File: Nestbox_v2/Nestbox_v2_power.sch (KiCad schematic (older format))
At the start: 47 parts, among them U201 bq25504, U202 TPS63051, U203 TPS63050

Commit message: created V2 MLX breakout board
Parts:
- removed BT201: Battery, Connectors_Molex:Molex_KK-6410-02_02x2.54mm_Straight, symbol Battery-RESCUE-Nestbox_v1
- removed C201, C202, C203: C, symbol C
- removed D201, D202: LED, symbol LED
- removed JP201: Jumper, symbol Jumper
- removed L201: L, symbol L
- removed R203, R206, R207, R208, R209, R210, R212, R213, R214, R221, R222: R, symbol R
- removed R211: 1E, symbol R
- removed SC201: Solar_Cells, symbol Solar_Cells
- removed U201: bq25504, symbol bq25504-RESCUE-Nestbox_v2
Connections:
- net labels removed: BAT_OK, HK_SOLAR_I
- wire segments 136 -> 102
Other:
- note removed: "OT_PROG to GND means 60° temp limit\nTO REVIEW"
- note removed: "is this for solar current measurement?\nmay be useful to use low-ohmic 4-terminal\n current sense resistor and a pre-amp"
- moved on the sheet: C204, C205, C206, C207, C208, C209, C210, JP202, JP203, JP204, JP205, L202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

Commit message: restructured top level sheet with hierarchical labels, assigned most GPIOs
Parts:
- removed R215, R216: R, symbol R
- added J?: CONN_01X02, symbol CONN_01X02
- added U?: LP5907, TO_SOT_Packages_SMD:SOT-23-5, symbol LD3985M
- R201, R202, R204, R205: value R -> 1M 1%
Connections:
- net labels added: +3V3, 5V_ENABLE, HK_5V_V, LDO_EN, VAA
- net labels removed: 5V_Enable, HK_BUS_V, HK_SOLAR_V, PGOOD_3.3, PGOOD_5, VBus, VSolar
- wire segments 102 -> 101
- no-connect marks 0 -> 1
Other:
- note added: "TODO: add battery undervoltage protection circuit!\n(to enable pin!)\n\nOther option: Use 2 cell alkaline battery."
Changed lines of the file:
@@
 LIBS:SeeedOPL-Transistor-2016
 LIBS:Nestbox_v2-cache
-EELAYER 26 0
+EELAYER 25 0
 EELAYER END
 $Descr A4 11693 8268
@@
 	3050 1700 2900 1700
 Wire Wire Line
-	2900 1700 2900 1900
-Wire Wire Line
 	2400 1900 2700 1900
 Wire Wire Line
 	2700 1900 2900 1900
 Wire Wire Line
-	2900 1900 3050 1900
+	2900 1900 2950 1900
+Wire Wire Line
+	2950 1900 3050 1900
 Connection ~ 2900 1900
 Text Label 1250 1900 0    60   ~ 0
-VBus
+VBat
 Wire Wire Line
 	3050 2400 3000 2400
@@
 	0    1    1    0
 $EndComp
-Text GLabel 4600 1350 2    60   Input ~ 0
-PGOOD_3.3
-Wire Wire Line
-	4500 1700 4500 1350
-Wire Wire Line
-	4500 1350 4600 1350
 Connection ~ 4500 1700
 Wire Wire Line
@@
 	6000 4150 6300 4150
 Connection ~ 4950 4150
-Wire Wire Line
-	4500 3950 4500 3600
-Wire Wire Line
-	4500 3600 4600 3600
 Connection ~ 4500 3950
 Wire Wire Line
@@
 	4450 4650 4550 4650
 Connection ~ 4550 4750
-Text GLabel 4600 3600 2    60   Input ~ 0
-PGOOD_5
 $Comp
 L +5V #PWR019
@@
 	5000 4750 4750 4750
 Connection ~ 4750 4750
-Text GLabel 2900 3950 0    60   Input ~ 0
-5V_Enable
 $Comp
 L C C205
@@
 	1800 4150 1550 4150
 Text Label 1550 4150 0    60   ~ 0
-VBus
+VBat
 $Comp
 L R R201
@@
 P 8650 1600
 F 0 "R201" H 8720 1646 50  0000 L CNN
-F 1 "R" H 8720 1555 50  0000 L CNN
+F 1 "1M 1%" H 8720 1555 50  0000 L CNN
 F 2 "" V 8580 1600 50  0001 C CNN
 F 3 "" H 8650 1600 50  0001 C CNN
@@
 P 8650 2000
 F 0 "R204" H 8720 2046 50  0000 L CNN
-F 1 "R" H 8720 1955 50  0000 L CNN
+F 1 "1M 1%" H 8720 1955 50  0000 L CNN
 F 2 "" V 8580 2000 50  0001 C CNN
 F 3 "" H 8650 2000 50  0001 C CNN
@@
 	1    0    0    -1
 $EndComp
-Wire Wire Line
-	8650 1150 8650 1450
 Wire Wire Line
 	8650 1750 8650 1800
@@
 	1    0    0    -1
 $EndComp
-Text GLabel 8800 1800 2    60   Input ~ 0
-HK_BUS_V
 Wire Wire Line
 	8650 1800 8800 1800
 Connection ~ 8650 1800
-Text Label 8650 1150 3    60   ~ 0
-VBus
 $Comp
 L R R202
@@
 P 9850 1600
 F 0 "R202" H 9920 1646 50  0000 L CNN
-F 1 "R" H 9920 1555 50  0000 L CNN
+F 1 "1M 1%" H 9920 1555 50  0000 L CNN
 F 2 "" V 9780 1600 50  0001 C CNN
 F 3 "" H 9850 1600 50  0001 C CNN
@@
 P 9850 2000
 F 0 "R205" H 9920 2046 50  0000 L CNN
-F 1 "R" H 9920 1955 50  0000 L CNN
+F 1 "1M 1%" H 9920 1955 50  0000 L CNN
 F 2 "" V 9780 2000 50  0001 C CNN
 F 3 "" H 9850 2000 50  0001 C CNN
@@
 	1    0    0    -1
 $EndComp
-Text GLabel 10000 1800 2    60   Input ~ 0
-HK_BAT_V
 Wire Wire Line
 	9850 1800 10000 1800
@@
 Text Label 9850 1150 3    60   ~ 0
 VBat
-$Comp
-L R R215
-U 1 1 5A02E91F
-P 9850 3000
-F 0 "R215" H 9920 3046 50  0000 L CNN
-F 1 "R" H 9920 2955 50  0000 L CNN
-F 2 "" V 9780 3000 50  0001 C CNN
-F 3 "" H 9850 3000 50  0001 C CNN
-	1    9850 3000
-	1    0    0    -1
-$EndComp
-$Comp
-L R R216
-U 1 1 5A02E925
-P 9850 3400
-F 0 "R216" H 9920 3446 50  0000 L CNN
-F 1 "R" H 9920 3355 50  0000 L CNN
-F 2 "" V 9780 3400 50  0001 C CNN
-F 3 "" H 9850 3400 50  0001 C CNN
-	1    9850 3400
-	1    0    0    -1
-$EndComp
-Wire Wire Line
-	9850 2550 9850 2850
-Wire Wire Line
-	9850 3150 9850 3200
-Wire Wire Line
-	9850 3200 9850 3250
-Wire Wire Line
-	9850 3550 9850 3600
-$Comp
-L GND #PWR025
-U 1 1 5A02E92E
-P 9850 3600
-F 0 "#PWR025" H 9850 3350 50  0001 C CNN
-F 1 "GND" H 9855 3427 50  0000 C CNN
-F 2 "" H 9850 3600 50  0001 C CNN
-F 3 "" H 9850 3600 50  0001 C CNN
-	1    9850 3600
-	1    0    0    -1
-$EndComp
-Text GLabel 10000 3200 2    60   Input ~ 0
-HK_SOLAR_V
-Wire Wire Line
-	9850 3200 10000 3200
-Connection ~ 9850 3200
-Text Label 9850 2550 3    60   ~ 0
-VSolar
+Text HLabel 2900 3950 0    60   Input ~ 0
+5V_ENABLE
+$Comp
+L +5V #PWR?
+U 1 1 5B070A76
+P 8650 1300
+F 0 "#PWR?" H 8650 1150 50  0001 C CNN
+F 1 "+5V" V 8665 1428 50  0000 L CNN
+F 2 "" H 8650 1300 50  0001 C CNN
+F 3 "" H 8650 1300 50  0001 C CNN
+	1    8650 1300
+	1    0    0    -1
+$EndComp
+Wire Wire Line
+	8650 1450 8650 1300
+Text HLabel 8800 1800 2    60   Input ~ 0
+HK_5V_V
+Text HLabel 10000 1800 2    60   Input ~ 0
+HK_BAT_V
+Text Notes 700  1450 0    60   ~ 0
+TODO: add battery undervoltage protection circuit!\n(to enable pin!)\n\nOther option: Use 2 cell alkaline battery.
+Wire Wire Line
+	2900 1700 2900 1900
+Wire Wire Line
+	2900 1900 2950 1900
+Connection ~ 2950 1900
+$Comp
+L CONN_01X02 J?
+U 1 1 5B072802
+P 8850 3200
+F 0 "J?" H 8850 3350 50  0000 C CNN
+F 1 "CONN_01X02" V 8950 3200 50  0000 C CNN
+F 2 "" H 8850 3200 50  0001 C CNN
+F 3 "" H 8850 3200 50  0001 C CNN
+	1    8850 3200
+	1    0    0    -1
+$EndComp
+Wire Wire Line
+	8650 3150 8350 3150
+Wire Wire Line
+	8650 3250 8400 3250
+Wire Wire Line
+	8400 3250 8400 3400
+$Comp
+L GND #PWR?
+U 1 1 5B072B3F
+P 8400 3400
+F 0 "#PWR?" H 8400 3150 50  0001 C CNN
+F 1 "GND" H 8400 3250 50  0000 C CNN
+F 2 "" H 8400 3400 50  0001 C CNN
+F 3 "" H 8400 3400 50  0001 C CNN
+	1    8400 3400
+	1    0    0    -1
+$EndComp
+Text Label 8350 3150 0    60   ~ 0
+VBat
+$Comp
+L LD3985M U?
+U 1 1 5B0757BD
+P 3600 6400
+F 0 "U?" H 3600 6715 50  0000 C CNN
+F 1 "LP5907" H 3600 6624 50  0000 C CNN
+F 2 "TO_SOT_Packages_SMD:SOT-23-5" H 3500 6150 50  0001 C CNN
+F 3 "" H 3600 6400 50  0001 C CNN
+	1    3600 6400
+	1    0    0    -1
+$EndComp
+$Comp
+L +3V3 #PWR?
+U 1 1 5B0757C4
+P 2900 6350
+F 0 "#PWR?" H 2900 6200 50  0001 C CNN
+F 1 "+3V3" H 2915 6523 50  0000 C CNN
+F 2 "" H 2900 6350 50  0001 C CNN
+F 3 "" H 2900 6350 50  0001 C CNN
+	1    2900 6350
+	1    0    0    -1
+$EndComp
+$Comp
+L GND #PWR?
+U 1 1 5B0757CA
+P 3600 6800
+F 0 "#PWR?" H 3600 6550 50  0001 C CNN
+F 1 "GND" H 3605 6627 50  0000 C CNN
+F 2 "" H 3600 6800 50  0001 C CNN
+F 3 "" H 3600 6800 50  0001 C CNN
+	1    3600 6800
+	1    0    0    -1
+$EndComp
+NoConn ~ 4100 6450
+$Comp
+L VAA #PWR?
+U 1 1 5B0757D1
+P 4350 6350
+F 0 "#PWR?" H 4350 6200 50  0001 C CNN
+F 1 "VAA" H 4367 6523 50  0000 C CNN
+F 2 "" H 4350 6350 50  0001 C CNN
+F 3 "" H 4350 6350 50  0001 C CNN
+	1    4350 6350
+	1    0    0    -1
+$EndComp
+Wire Wire Line
+	2900 6350 3100 6350
+Wire Wire Line
+	3100 6450 2900 6450
+Wire Wire Line
+	4100 6350 4350 6350
+Text HLabel 2900 6450 0    60   Input ~ 0
+LDO_EN
 $EndSCHEMATC

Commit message: finished power supply schematics
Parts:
- removed C206: 10u, symbol C
- removed C210: 10p, symbol C
- removed R201, R202, R204, R205: 1M 1%, symbol R
- removed R217: 1M, symbol R
- removed U202: TPS63051, symbol TPS63051
- removed U203: TPS63050, symbol TPS63050
- added C? (x2): 1u, symbol C
- added R?: 100k, symbol R
- added R?: 50k, symbol R
- added U?: TPS62745, symbol TPS62745
- added U?: TPS62125, symbol TPS62125
- L203: value 1.5u -> 10uH
- R219: value R -> 1M1
- R220: value R -> 210k
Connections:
- net labels added: +BATT, 5V_PG, BAT_TEST_ENABLE, Vbat
- net labels removed: HK_5V_V
- wire segments 101 -> 81
- no-connect marks 1 -> 3
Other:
- note removed: "ILIM0 = Low <- 0.65*Iin_max"
- note removed: "SS floating for default Soft-Start time"
- moved on the sheet: C204, JP202, L202, L203, R218, R220

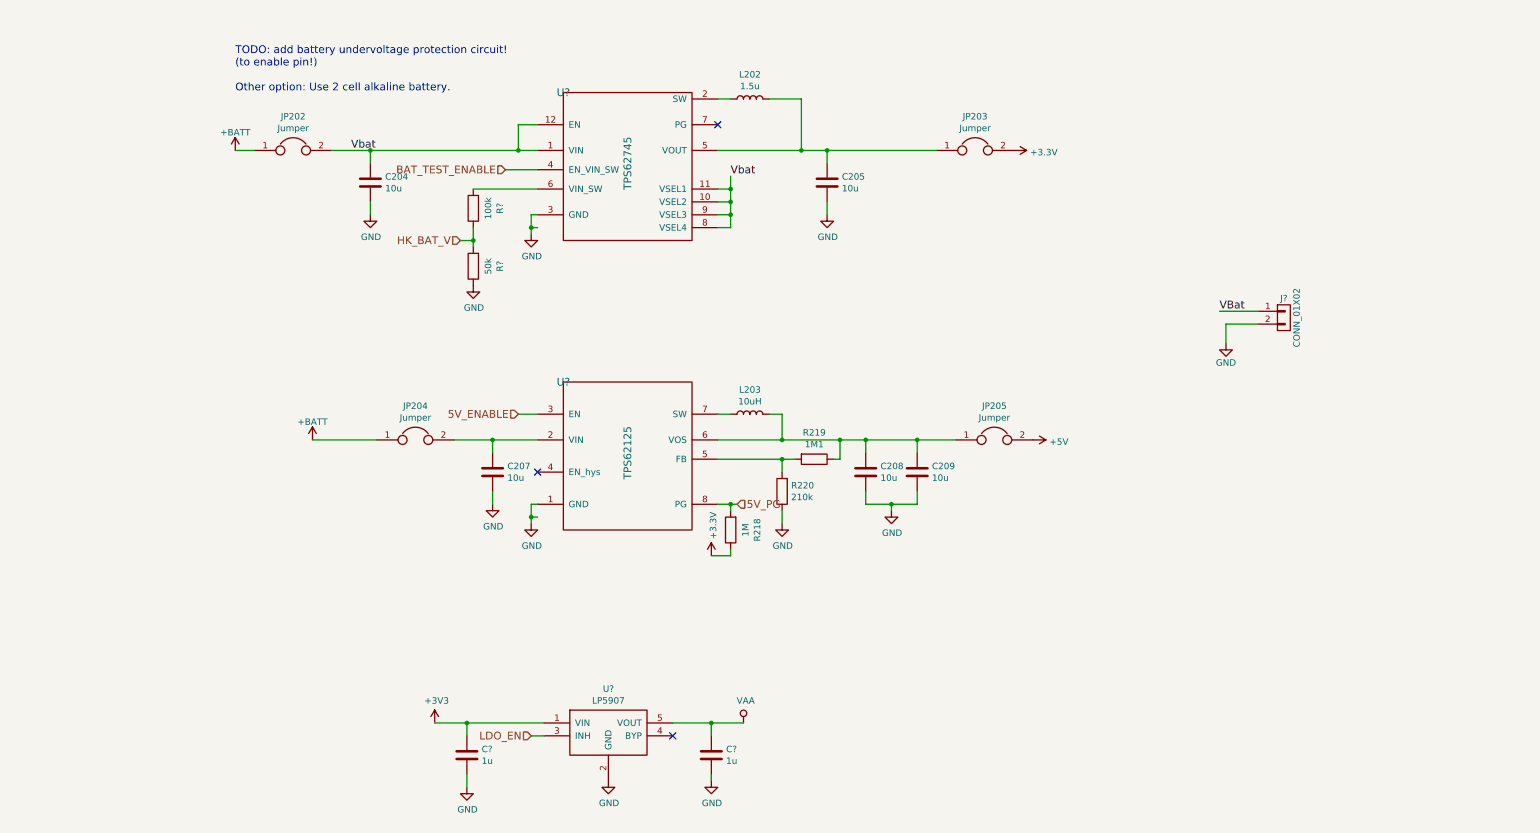
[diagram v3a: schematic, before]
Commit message: added PIR and lightbarrier headers
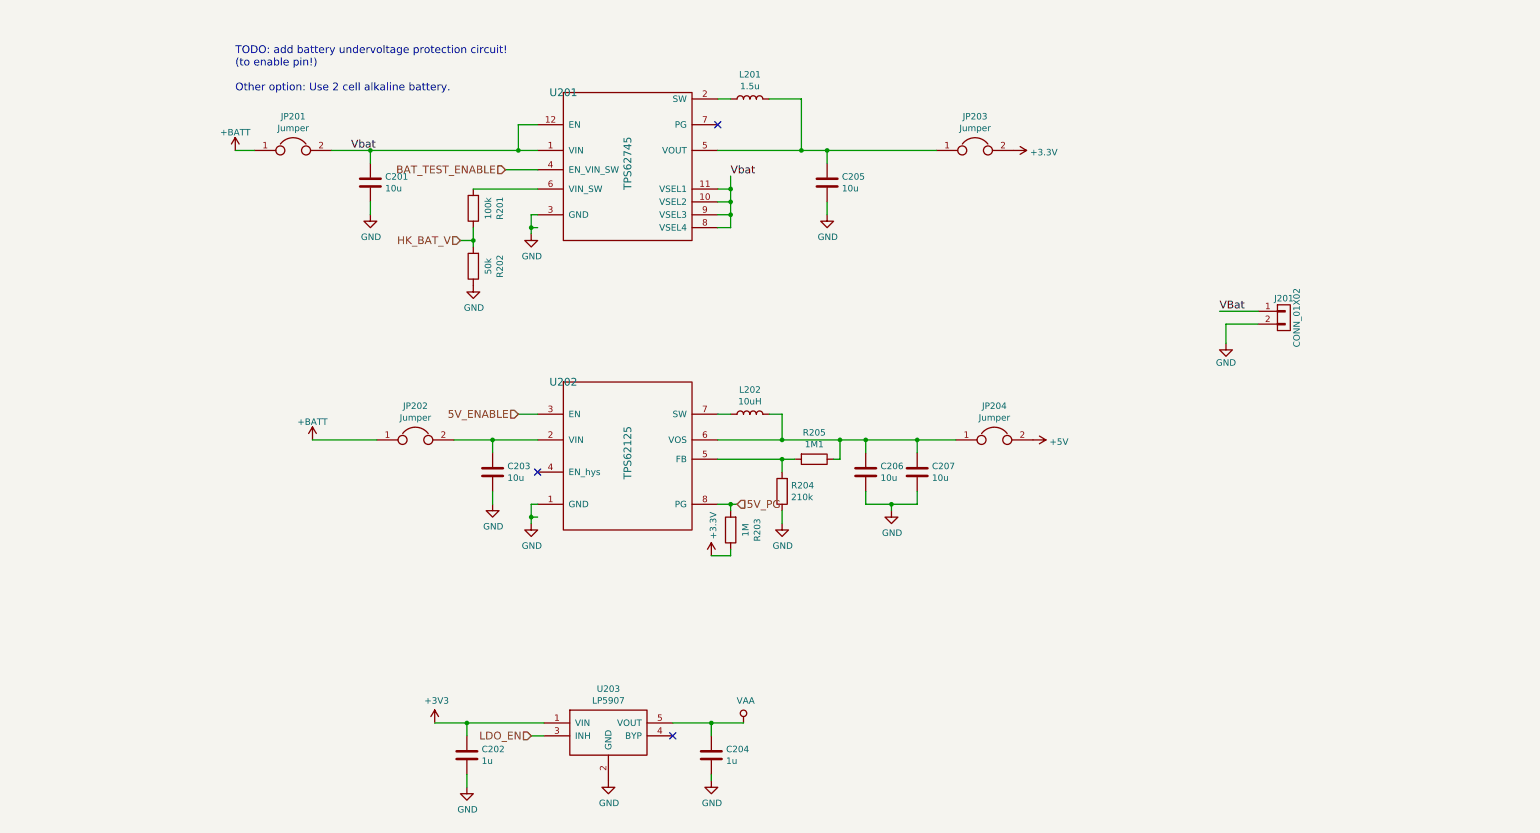
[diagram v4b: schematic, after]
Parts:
- gave numbers to parts that had none: 8
- renumbered C204 to C201, C207 to C203, C208 to C206, C209 to C207, JP202 to JP201, JP204 to JP202, JP205 to JP204, L202 to L201, L203 to L202, R218 to R203, R220 to R204, R219 to R205

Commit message: added power footprints, final connector footprints
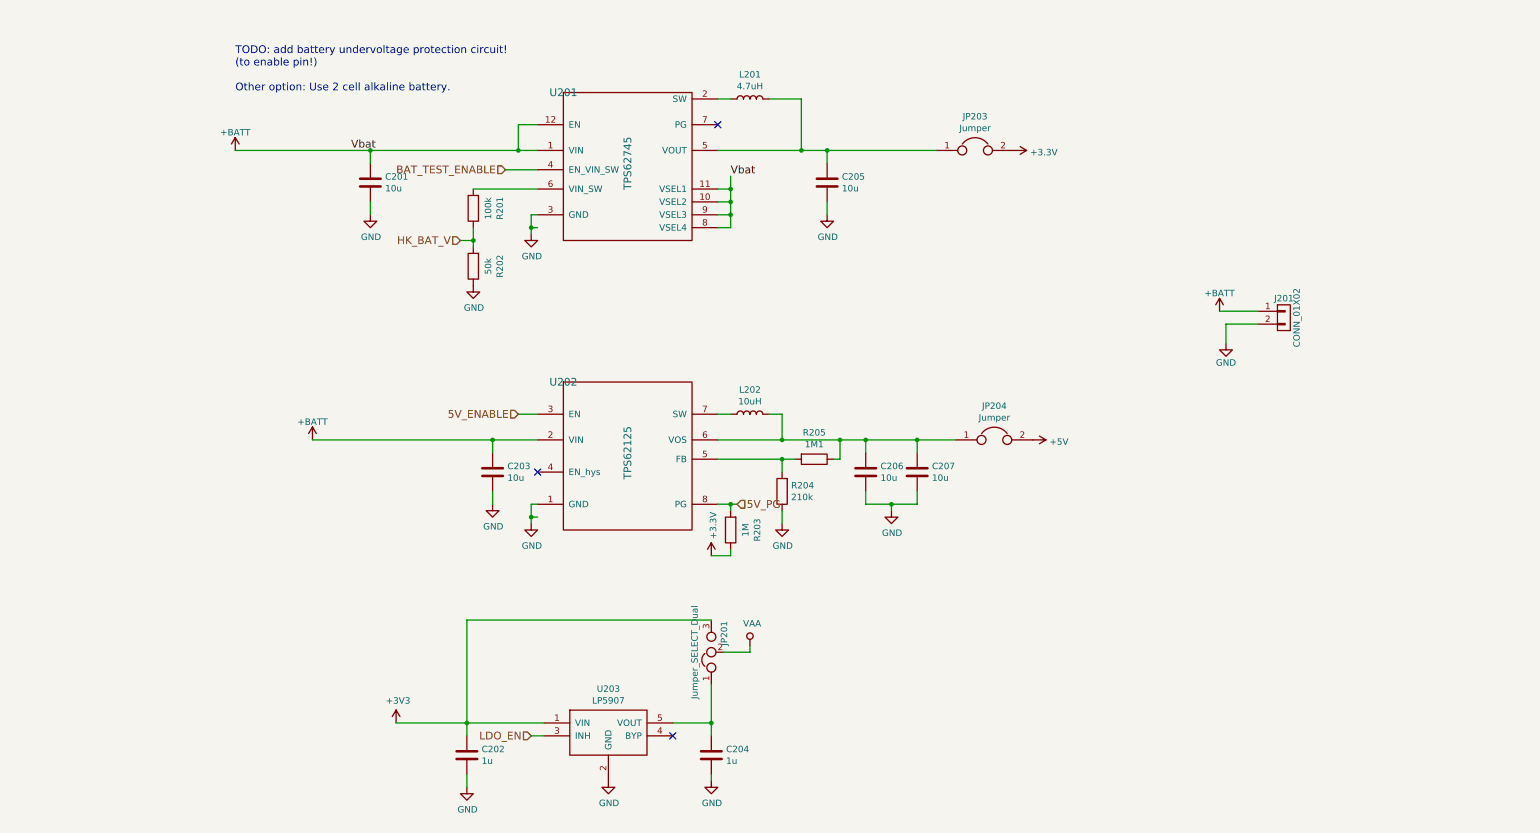
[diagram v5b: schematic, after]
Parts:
- removed JP201, JP202: Jumper, symbol Jumper
- added JP201: Jumper_SELECT_Dual, Pin_Headers:Pin_Header_Straight_1x03, symbol Jumper_SELECT_Dual
- C201, C202, C203, C204, C205, C206, C207: footprint (none) -> Capacitors_SMD:C_0603
- J201: footprint (none) -> Terminal_Blocks:TerminalBlock_Pheonix_PT-3.5mm_2pol
- JP203, JP204: footprint (none) -> Pin_Headers:Pin_Header_Straight_1x02
- L201: value 1.5u -> 4.7uH
- R201, R202, R203, R204, R205: footprint (none) -> Resistors_SMD:R_0603
- U201: footprint (none) -> Octanis3:WSON_3x2mm_12pin
- U202: footprint (none) -> Octanis3:WSON_2x2mm_8pin
- U203: footprint TO_SOT_Packages_SMD:SOT-23-5 -> texasinstruments:SOT23-5
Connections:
- net VBat is gone; now on net +BATT: J201.1 (P1)
- net Vbat is gone; now on net +BATT: C201.1, U201.1 (VIN), U201.10 (VSEL2), U201.11 (VSEL1), U201.12 (EN), U201.8 (VSEL4), U201.9 (VSEL3)
- net +3V3: now also JP201.3
- net +BATT: now also C203.1, U202.2 (VIN)
- net VAA: now also JP201.2; no longer C204.1, U203.5 (VOUT)
- new net: C204.1, JP201.1, U203.5 (VOUT)
